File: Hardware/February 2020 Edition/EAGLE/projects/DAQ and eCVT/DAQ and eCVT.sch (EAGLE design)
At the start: 85 parts

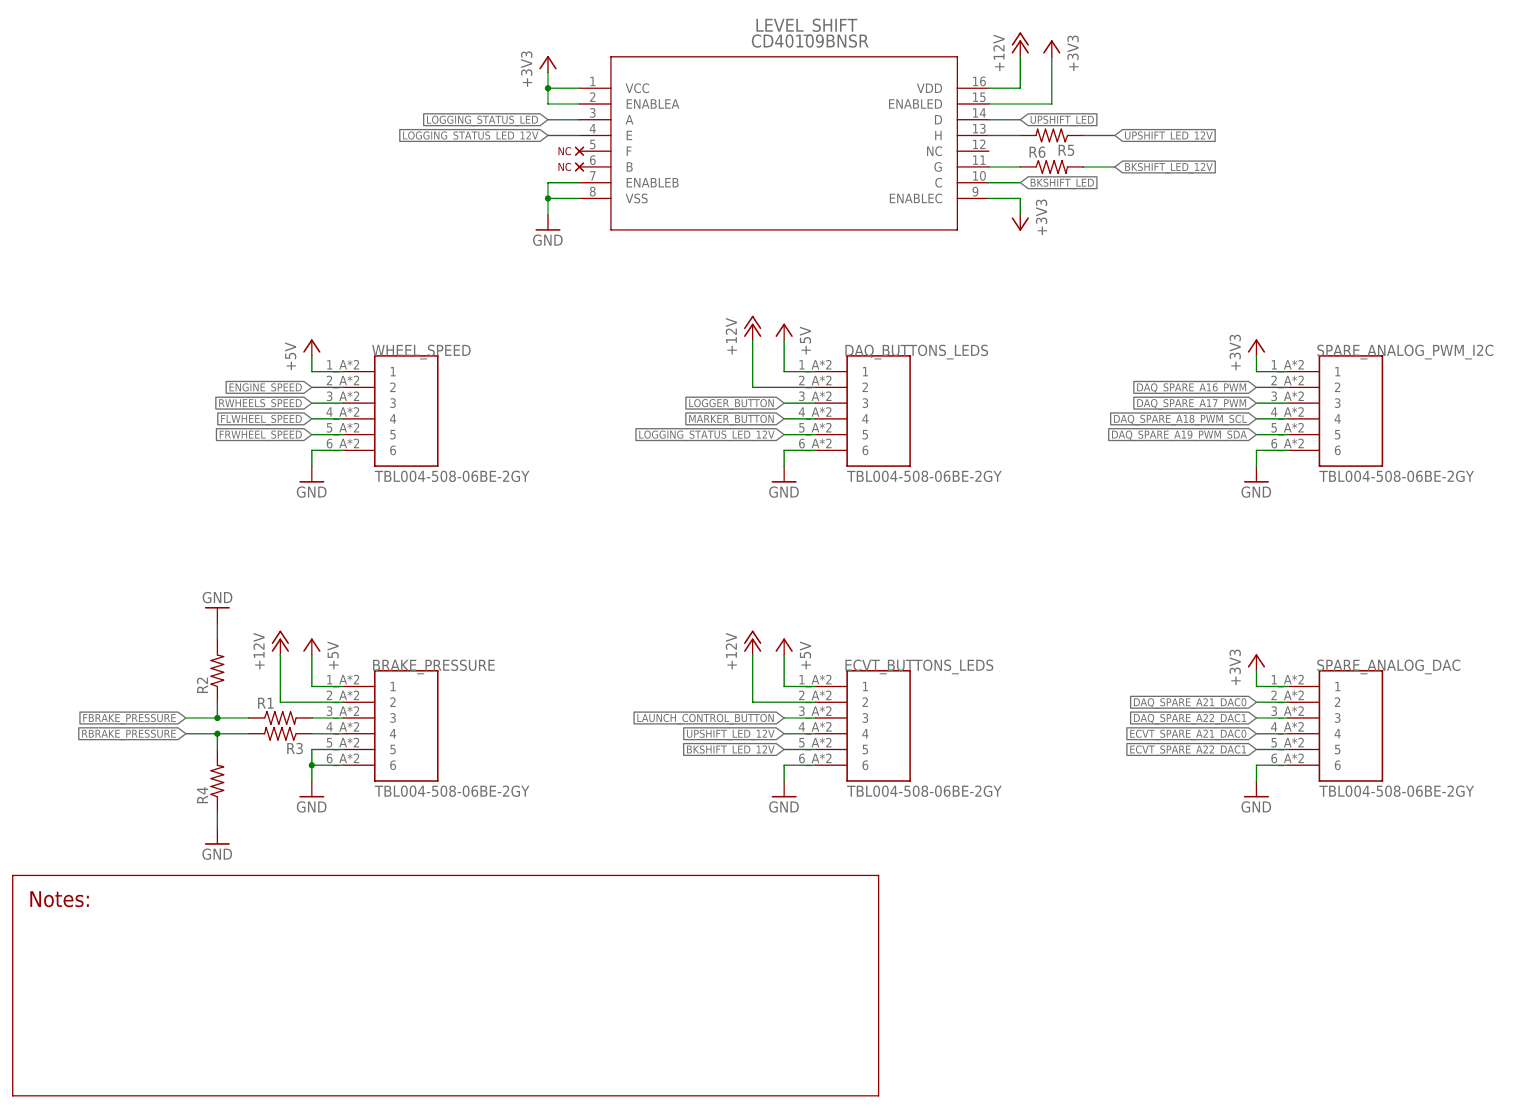
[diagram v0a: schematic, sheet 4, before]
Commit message: Finished schematic except RJ45 connectors and LEDs, need to redo board
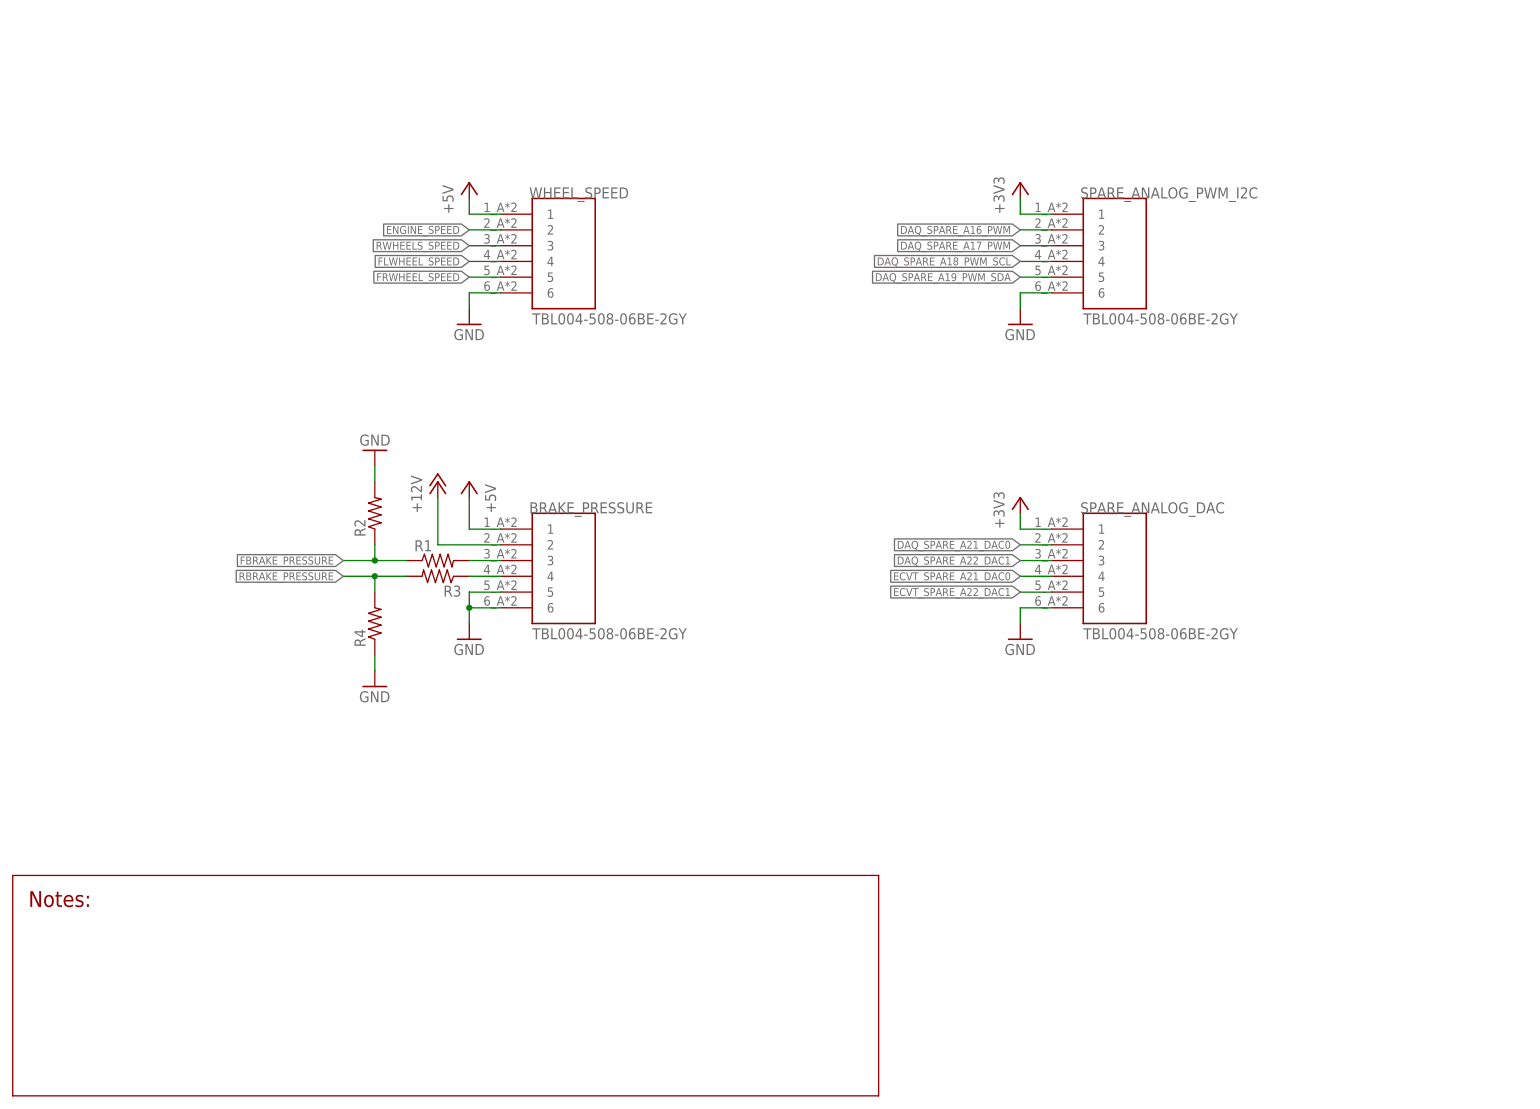
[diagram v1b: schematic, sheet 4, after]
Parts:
- removed DAQ, ECVT: TEENSY_3.5, Teensy:TEENSY_3.5
- removed DAQ_BUTTONS_LEDS, ECVT_BUTTONS_LEDS: TBL004-508-06BE-2GY, Screwless Terminal 6-Pole:TBL004-508-06BE-2GY
- removed MOTOR_DRIVER: POLOLU_DUAL_VNH5019, Pololo Dual VNH5019:POLOLU_DUAL_VNH5019
- removed PENC, SENC: SHF-105-01-X-D-TH, Male Header 2x5 0.05in:SHF-105-01-X-D-TH
- removed R5, R6: (no value), rcl:R-US_0204/7
- removed U$18, U$19, U$20, U$21, U$36, U$37, U$38, U$39: NC, ME507:NC
- removed U$59, U$60, U$61, U$62, U$63, U$64, U$65, U$66, U$67, U$68: NC, ME 507:NC
- removed USB: UJ2-MIBH2-4-SMT-TR, Micro USB:UJ2-MIBH2-4-SMT-TR
- removed VOLT_REG: LD1117V33, Voltage Regulator 3.3V:LD1117V33
- added U$33: TEENSY_3.5_BAJA, Teensy:TEENSY_3.5_BAJA
- added U1: AP2114H-3.3TRG1, Voltage Regulator 3.3V:AP2114H-3.3TRG1
- C1: value 0.1uF -> 4.7uF
- C2: value 10uF -> 4.7uF
- U$28: value NC -> POLOLU_DUAL_VNH5019_BAJA; device ME507:NC -> Pololo Dual VNH5019:POLOLU_DUAL_VNH5019_BAJA
- U$31: value NC -> TEENSY_3.5_BAJA; device ME507:NC -> Teensy:TEENSY_3.5_BAJA
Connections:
- removed net BACKSHIFT_LED_12V_W/O_RES: LEVEL_SHIFT.G, R6.1
- removed net LAUNCH_CONTROL_BUTTON: ECVT_BUTTONS_LEDS.3
- removed net LOGGING_STATUS_LED: LEVEL_SHIFT.A
- removed net LOGGING_STATUS_LED_12V: DAQ_BUTTONS_LEDS.5, LEVEL_SHIFT.E
- removed net N$35: ECVT.35/A16, U$24.D
- removed net N$36: ECVT.36/A17, U$25.D
- removed net N$37: ECVT.37/A18, U$26.D
- removed net N$38: ECVT.38/A19, U$27.D
- removed net N$39: U$30.D, USB.4
- removed net N$40: U$31.D, USB.SHIELD
- removed net N$41: ECVT.4/CANRX, U$1.D
- removed net N$54: ECVT.VIN, U$55.D
- removed net N$55: DAQ.VIN, U$56.D
- removed net N$56: PENC.9, U$61.D
- removed net N$58: LEVEL_SHIFT.F, U$67.D
- removed net N$59: PENC.10, U$62.D
- removed net N$60: LEVEL_SHIFT.B, U$68.D
- removed net N$64: PENC.4, U$59.D
- removed net N$65: PENC.1, U$60.D
- removed net N$68: SENC.4, U$63.D
- removed net N$69: SENC.10, U$64.D
- removed net N$70: SENC.1, U$65.D
- removed net N$71: SENC.9, U$66.D
- removed net UPSHIFT_LED_12V_W/O_RES: LEVEL_SHIFT.H, R5.2
- new net DAQ_STATUS_LED_12V: LEVEL_SHIFT.E
- new net ECVT_STATUS_LED_12V: LEVEL_SHIFT.F
- new net N$33: U$32.D, U$33.32/A13
- net +12V: now also U$28.VOUT; no longer DAQ_BUTTONS_LEDS.2, ECVT_BUTTONS_LEDS.2, MOTOR_DRIVER.VOUT
- net +3V3: now also U$28.M1EN, U$28.M2EN, U$28.VDD, U$31.3V3_LO, U$33.3V3_LO, U1.VOUT; no longer DAQ.3V3, DAQ.3V3_LO, ECVT.3V3, ECVT.3V3_LO, MOTOR_DRIVER.3V3, MOTOR_DRIVER.M1EN, MOTOR_DRIVER.M2EN, MOTOR_DRIVER.VDD, VOLT_REG.OUTPUT
- net +5V: now also U1.VIN; no longer DAQ_BUTTONS_LEDS.1, ECVT_BUTTONS_LEDS.1, MOTOR_DRIVER.5V, PENC.2, SENC.2, USB.1, VOLT_REG.INPUT
- net BKSHIFT_LED: now also U$33.1/TX; no longer ECVT.1/TX
- net BKSHIFT_LED_12V: now also LEVEL_SHIFT.G; no longer ECVT_BUTTONS_LEDS.5, R6.2
- net DAQ_ECVT\_CS: now also U$31.15/A1; no longer DAQ.15/A1
- net DAQ_ECVT\_MISO: now also U$31.12/MISO; no longer DAQ.12/MISO
- net DAQ_ECVT_CS: now also U$33.15/A1; no longer ECVT.15/A1
- net DAQ_ECVT_MISO: now also U$33.12/MISO; no longer ECVT.12/MISO
- net DAQ_ECVT_MOSI: now also U$31.11/MOSI, U$33.11/MOSI; no longer DAQ.11/MOSI, ECVT.11/MOSI
- net DAQ_ECVT_RX: now also U$31.9/CS, U$33.10/CS; no longer DAQ.9/CS, ECVT.10/CS
- net DAQ_ECVT_SCK: now also U$31.14/A0, U$33.14/A0; no longer DAQ.14/A0, ECVT.14/A0
- net DAQ_ECVT_TX: now also U$31.10/CS, U$33.9/CS; no longer DAQ.10/CS, ECVT.9/CS
- net DAQ_SPARE_A16_PWM: now also U$31.35/A16; no longer DAQ.35/A16
- net DAQ_SPARE_A17_PWM: now also U$31.36/A17; no longer DAQ.36/A17
- net DAQ_SPARE_A18_PWM_SCL: now also U$31.37/A18; no longer DAQ.37/A18
- net DAQ_SPARE_A19_PWM_SDA: now also U$31.38/A19; no longer DAQ.38/A19
- net DAQ_SPARE_A21_DAC0: now also U$31.A21/DAC0; no longer DAQ.A21/DAC0
- net DAQ_SPARE_A22_DAC1: now also U$31.A22/DAC1; no longer DAQ.A22/DAC1
- net DAQ_STATUS_LED: now also LEVEL_SHIFT.A, U$31.2; no longer DAQ.2
- net DAQ_XBEE_CS: now also U$31.31/A12; no longer DAQ.31/A12
- net DAQ_XBEE_MISO: now also U$31.1/TX; no longer DAQ.1/TX
- net DAQ_XBEE_MOSI: now also U$31.0/RX; no longer DAQ.0/RX
- net DAQ_XBEE_RX: now also U$31.7; no longer DAQ.7
- net DAQ_XBEE_SCK: now also U$31.32/A13; no longer DAQ.32/A13
- net DAQ_XBEE_TX: now also U$31.8; no longer DAQ.8
- net ECVT_SPARE_A21_DAC0: now also U$33.A21/DAC0; no longer ECVT.A21/DAC0
- net ECVT_SPARE_A22_DAC1: now also U$33.A22/DAC1; no longer ECVT.A22/DAC1
- net ECVT_STATUS_LED: now also LEVEL_SHIFT.B, U$33.2; no longer ECVT.2
- net ENGINE_SPEED: now also U$31.5, U$33.5; no longer DAQ.5, ECVT.5
- net FBRAKE_PRESSURE: now also U$31.33/A14, U$33.33/A14; no longer DAQ.33/A14, ECVT.33/A14
- net FLWHEEL_SPEED: now also U$31.29, U$33.29; no longer DAQ.29, ECVT.29
- net FRWHEEL_SPEED: now also U$31.30, U$33.30; no longer DAQ.30, ECVT.30
- net GND: now also U$28.GND, U$31.AGND, U$31.GND, U$31.GND2, U$33.AGND, U$33.GND, U$33.GND2, U1.GND; no longer DAQ.AGND, DAQ.GND, DAQ.GND2, DAQ_BUTTONS_LEDS.6, ECVT.AGND, ECVT.GND, ECVT.GND2, ECVT_BUTTONS_LEDS.6, MOTOR_DRIVER.GND, MOTOR_DRIVER.GND1, MOTOR_DRIVER.GND2, MOTOR_DRIVER.GND3, PENC.3, SENC.3, USB.5, VOLT_REG.GROUND
- net LAUNCH_BUTTON: now also U$33.3/CANTX; no longer ECVT.3/CANTX
- net LOGGER_BUTTON: now also U$31.3/CANTX; no longer DAQ.3/CANTX, DAQ_BUTTONS_LEDS.3
- net MARKER_BUTTON: now also U$31.4/CANRX; no longer DAQ.4/CANRX, DAQ_BUTTONS_LEDS.4
- net N$1: now also U$29.D, U1.VOUT_2; no longer U$28.D, USB.2
- net N$10: now also U$11.D, U$31.22/A8; no longer DAQ.23/A9, U$12.D
- net N$11: now also U$12.D, U$31.23/A9; no longer DAQ.24, U$13.D
- net N$12: now also U$13.D, U$31.24; no longer DAQ.25, U$14.D
- net N$13: now also U$14.D, U$31.25; no longer DAQ.26, U$15.D
- net N$14: now also U$15.D, U$31.26; no longer DAQ.27, U$16.D
- net N$15: now also U$16.D, U$31.27; no longer DAQ.28, U$17.D
- net N$16: now also U$17.D, U$31.28; no longer DAQ.VUSB, U$18.D
- net N$17: now also U$22.D, U$31.39/A20; no longer DAQ.AREF, U$19.D
- net N$18: now also U$31.VIN, U$56.D; no longer DAQ.A10, U$20.D
- net N$19: now also U$33.3V3; no longer DAQ.A11, U$21.D
- net N$2: now also U$31.3V3; no longer DAQ.13/SCK, U$4.D
- net N$20: now also U$3.D, U$33.13/SCK; no longer DAQ.39/A20, U$22.D
- net N$21: now also LEVEL_SHIFT.NC, U$30.D; no longer U$29.D, USB.3
- net N$22: now also U$33.39/A20, U$40.D; no longer ECVT.13/SCK, U$3.D
- net N$23: now also U$33.7, U$41.D; no longer ECVT.VUSB, U$36.D
- net N$24: now also U$33.8, U$42.D; no longer ECVT.28, U$23.D
- net N$25: now also U$23.D, U$33.28; no longer ECVT.AREF, U$37.D
- net N$26: now also U$24.D, U$33.35/A16; no longer ECVT.A10, U$38.D
- net N$27: now also U$25.D, U$33.36/A17; no longer ECVT.A11, U$39.D
- net N$28: now also U$26.D, U$33.37/A18; no longer ECVT.39/A20, U$40.D
- net N$29: now also U$27.D, U$33.38/A19; no longer ECVT.7, U$41.D
- net N$3: now also U$31.13/SCK, U$4.D; no longer DAQ.16/A2, U$5.D
- net N$30: now also U$33.VIN, U$55.D; no longer ECVT.8, U$42.D
- net N$31: now also U$1.D, U$33.4/CANRX; no longer ECVT.31/A12, U$2.D
- net N$32: now also U$2.D, U$33.31/A12; no longer ECVT.32/A13, U$32.D
- net N$4: now also U$31.16/A2, U$5.D; no longer DAQ.17/A3, U$6.D
- net N$5: now also U$31.17/A3, U$6.D; no longer DAQ.18/A4/SDA, U$7.D
- net N$6: now also U$31.18/A4/SDA, U$7.D; no longer DAQ.19/A5/SCL, U$8.D
- net N$7: now also U$31.19/A5/SCL, U$8.D; no longer DAQ.20/A6, U$9.D
- net N$8: now also U$31.20/A6, U$9.D; no longer DAQ.21/A7, U$10.D
- net N$9: now also U$10.D, U$31.21/A7; no longer DAQ.22/A8, U$11.D
- net PENC_A: now also U$33.24; no longer ECVT.24
- net PENC_B: now also U$33.25; no longer ECVT.25
- net PENC_CHA: no longer PENC.6
- net PENC_CHA/: no longer PENC.5
- net PENC_CHB: no longer PENC.8
- net PENC_CHB/: no longer PENC.7
- net PMOT_CS: now also U$28.M1CS, U$33.16/A2; no longer ECVT.16/A2, MOTOR_DRIVER.M1CS
- net PMOT_INA: now also U$28.M1INA, U$33.18/A4/SDA; no longer ECVT.18/A4/SDA, MOTOR_DRIVER.M1INA
- net PMOT_INB: now also U$28.M1INB, U$33.19/A5/SCL; no longer ECVT.19/A5/SCL, MOTOR_DRIVER.M1INB
- net PMOT_PWM: now also U$28.M1PWM, U$33.22/A8; no longer ECVT.22/A8, MOTOR_DRIVER.M1PWM
- net RBRAKE_PRESSURE: now also U$31.34/A15, U$33.34/A15; no longer DAQ.34/A15, ECVT.34/A15
- net RWHEELS_SPEED: now also U$31.6, U$33.6; no longer DAQ.6, ECVT.6
- net SENC_A: now also U$33.26; no longer ECVT.26
- net SENC_B: now also U$33.27; no longer ECVT.27
- net SENC_CHA: no longer SENC.6
- net SENC_CHA/: no longer SENC.5
- net SENC_CHB: no longer SENC.8
- net SENC_CHB/: no longer SENC.7
- net SMOT_CS: now also U$28.M2CS, U$33.17/A3; no longer ECVT.17/A3, MOTOR_DRIVER.M2CS
- net SMOT_INA: now also U$28.M2INA, U$33.20/A6; no longer ECVT.20/A6, MOTOR_DRIVER.M2INA
- net SMOT_INB: now also U$28.M2INB, U$33.21/A7; no longer ECVT.21/A7, MOTOR_DRIVER.M2INB
- net SMOT_PWM: now also U$28.M2PWM, U$33.23/A9; no longer ECVT.23/A9, MOTOR_DRIVER.M2PWM
- net UPSHIFT_LED: now also U$33.0/RX; no longer ECVT.0/RX
- net UPSHIFT_LED_12V: now also LEVEL_SHIFT.H; no longer ECVT_BUTTONS_LEDS.4, R5.1
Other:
- moved on the sheet: BRAKE_PRESSURE, C1, C2, DIFF_LINE_REC, R1, R2, R3, R4, SPARE_ANALOG_DAC, SPARE_ANALOG_PWM_I2C, WHEEL_SPEED, XBEE

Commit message: Finished schematic, need to check LED wiring
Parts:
- removed SPARE_ANALOG_DAC, SPARE_ANALOG_PWM_I2C: TBL004-508-06BE-2GY, Screwless Terminal 6-Pole:TBL004-508-06BE-2GY
- added D1: LTST-C170TBKT, LED:LTST-C170TBKT
- added J1, J2, J3, J4: 5558342-1, RJ45:5558342-1
- added R5: (no value), rcl:R-US_R0805
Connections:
- new net N$34: D1.-, R5.1
- new net PENC_CHI: J1.1
- new net PENC_CHI/: J1.2
- new net SENC_CHI: J2.1
- new net SENC_CHI/: J2.2
- net +12V: no longer BRAKE_PRESSURE.2
- net +3V3: now also BRAKE_PRESSURE.1, D1.+; no longer SPARE_ANALOG_DAC.1, SPARE_ANALOG_PWM_I2C.1
- net +5V: now also BRAKE_PRESSURE.2, J1.7, J2.7; no longer BRAKE_PRESSURE.1
- net BKSHIFT_LED_12V: now also J3.3
- net DAQ_SPARE_A16_PWM: now also J4.1; no longer SPARE_ANALOG_PWM_I2C.2
- net DAQ_SPARE_A17_PWM: now also J4.2; no longer SPARE_ANALOG_PWM_I2C.3
- net DAQ_SPARE_A18_PWM_SCL: now also J4.3; no longer SPARE_ANALOG_PWM_I2C.4
- net DAQ_SPARE_A19_PWM_SDA: now also J4.4; no longer SPARE_ANALOG_PWM_I2C.5
- net DAQ_SPARE_A21_DAC0: now also J4.5; no longer SPARE_ANALOG_DAC.2
- net DAQ_SPARE_A22_DAC1: now also J4.6; no longer SPARE_ANALOG_DAC.3
- net DAQ_STATUS_LED_12V: now also J3.2
- net ECVT_SPARE_A21_DAC0: now also J4.7; no longer SPARE_ANALOG_DAC.4
- net ECVT_SPARE_A22_DAC1: now also J4.8; no longer SPARE_ANALOG_DAC.5
- net ECVT_STATUS_LED_12V: now also J3.5
- net GND: now also J1.8, J2.8, J3.8, R5.2; no longer SPARE_ANALOG_DAC.6, SPARE_ANALOG_PWM_I2C.6
- net LAUNCH_BUTTON: now also J3.4
- net LOGGER_BUTTON: now also J3.1
- net MARKER_BUTTON: now also J3.7
- net PENC_CHA: now also J1.3
- net PENC_CHA/: now also J1.6
- net PENC_CHB: now also J1.4
- net PENC_CHB/: now also J1.5
- net SENC_CHA: now also J2.3
- net SENC_CHA/: now also J2.6
- net SENC_CHB: now also J2.4
- net SENC_CHB/: now also J2.5
- net UPSHIFT_LED_12V: now also J3.6

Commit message: Started board
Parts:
- removed U$29: NC, ME507:NC
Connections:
- removed net N$1: U$29.D, U1.VOUT_2
- net +3V3: now also U1.VOUT_2
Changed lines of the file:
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@@
 <part name="U1" library="Voltage Regulator 3.3V" deviceset="AP2114H-3.3TRG1" device=""/>
 <part name="GND7" library="supply1" library_urn="urn:adsk.eagle:library:371" deviceset="GND" device=""/>
-<part name="U$29" library="ME507" deviceset="NC" device=""/>
 <part name="P+2" library="supply1" library_urn="urn:adsk.eagle:library:371" deviceset="+5V" device=""/>
 <part name="+3V7" library="supply1" library_urn="urn:adsk.eagle:library:371" deviceset="+3V3" device=""/>
@@
 <part name="+3V9" library="supply1" library_urn="urn:adsk.eagle:library:371" deviceset="+3V3" device=""/>
 <part name="P+3" library="supply1" library_urn="urn:adsk.eagle:library:371" deviceset="+5V" device=""/>
+<part name="+3V10" library="supply1" library_urn="urn:adsk.eagle:library:371" deviceset="+3V3" device=""/>
 </parts>
 <sheets>
@@
 <attribute name="VALUE" x="45.4406" y="153.8986" size="2.0828" layer="96" ratio="6" rot="SR0"/>
 </instance>
-<instance part="GND7" gate="1" x="27.94" y="142.24" smashed="yes">
-<attribute name="VALUE" x="25.4" y="139.7" size="1.778" layer="96"/>
-</instance>
-<instance part="U$29" gate="A" x="33.02" y="144.78" smashed="yes" rot="R180"/>
+<instance part="GND7" gate="1" x="22.86" y="139.7" smashed="yes">
+<attribute name="VALUE" x="20.32" y="137.16" size="1.778" layer="96"/>
+</instance>
 <instance part="P+2" gate="1" x="88.9" y="124.46" smashed="yes" rot="R180">
 <attribute name="VALUE" x="91.44" y="129.54" size="1.778" layer="96" rot="R270"/>
@@
 <attribute name="NAME" x="201.93" y="153.8986" size="1.778" layer="95"/>
 <attribute name="VALUE" x="201.93" y="149.098" size="1.778" layer="96"/>
+</instance>
+<instance part="+3V10" gate="G$1" x="27.94" y="139.7" smashed="yes" rot="R180">
+<attribute name="VALUE" x="30.48" y="144.78" size="1.778" layer="96" rot="R270"/>
 </instance>
 </instances>
@@
 <pinref part="U1" gate="A" pin="GND"/>
 <pinref part="GND7" gate="1" pin="GND"/>
-<wire x1="33.02" y1="147.32" x2="27.94" y2="147.32" width="0.1524" layer="91"/>
-<wire x1="27.94" y1="147.32" x2="27.94" y2="144.78" width="0.1524" layer="91"/>
+<wire x1="33.02" y1="147.32" x2="22.86" y2="147.32" width="0.1524" layer="91"/>
+<wire x1="22.86" y1="147.32" x2="22.86" y2="142.24" width="0.1524" layer="91"/>
 </segment>
 <segment>
@@
 <wire x1="182.88" y1="152.4" x2="187.96" y2="152.4" width="0.1524" layer="91"/>
 </segment>
+<segment>
+<pinref part="U1" gate="A" pin="VOUT_2"/>
+<wire x1="33.02" y1="144.78" x2="27.94" y2="144.78" width="0.1524" layer="91"/>
+<wire x1="27.94" y1="144.78" x2="27.94" y2="142.24" width="0.1524" layer="91"/>
+<pinref part="+3V10" gate="G$1" pin="+3V3"/>
+</segment>
 </net>
 <net name="PMOT_INA" class="0">
@@
 </segment>
 </net>
-<net name="N$1" class="0">
-<segment>
-<pinref part="U$29" gate="A" pin="D"/>
-<pinref part="U1" gate="A" pin="VOUT_2"/>
-</segment>
-</net>

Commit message: Wiring the board...
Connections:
- removed net DAQ_ECVT\_CS: U$31.15/A1
- net DAQ_ECVT_CS: now also U$31.15/A1
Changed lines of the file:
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@@
 <?xml version="1.0" encoding="utf-8"?>
 <!DOCTYPE eagle SYSTEM "eagle.dtd">
-<eagle version="9.5.2">
+<eagle version="9.5.0">
 <drawing>
 <settings>
@@
 <pinref part="U$33" gate="G$1" pin="15/A1"/>
 </segment>
+<segment>
+<wire x1="91.44" y1="109.22" x2="86.36" y2="109.22" width="0.1524" layer="91"/>
+<label x="91.44" y="109.22" size="1.27" layer="95" xref="yes"/>
+<pinref part="U$31" gate="G$1" pin="15/A1"/>
+</segment>
 </net>
 <net name="DAQ_ECVT_SCK" class="0">
@@
 </segment>
 </net>
-<net name="DAQ_ECVT\_CS" class="0">
-<segment>
-<wire x1="91.44" y1="109.22" x2="86.36" y2="109.22" width="0.1524" layer="91"/>
-<label x="91.44" y="109.22" size="1.27" layer="95" xref="yes"/>
-<pinref part="U$31" gate="G$1" pin="15/A1"/>
-</segment>
-</net>
